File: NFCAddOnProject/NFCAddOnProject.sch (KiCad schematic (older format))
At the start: 30 parts

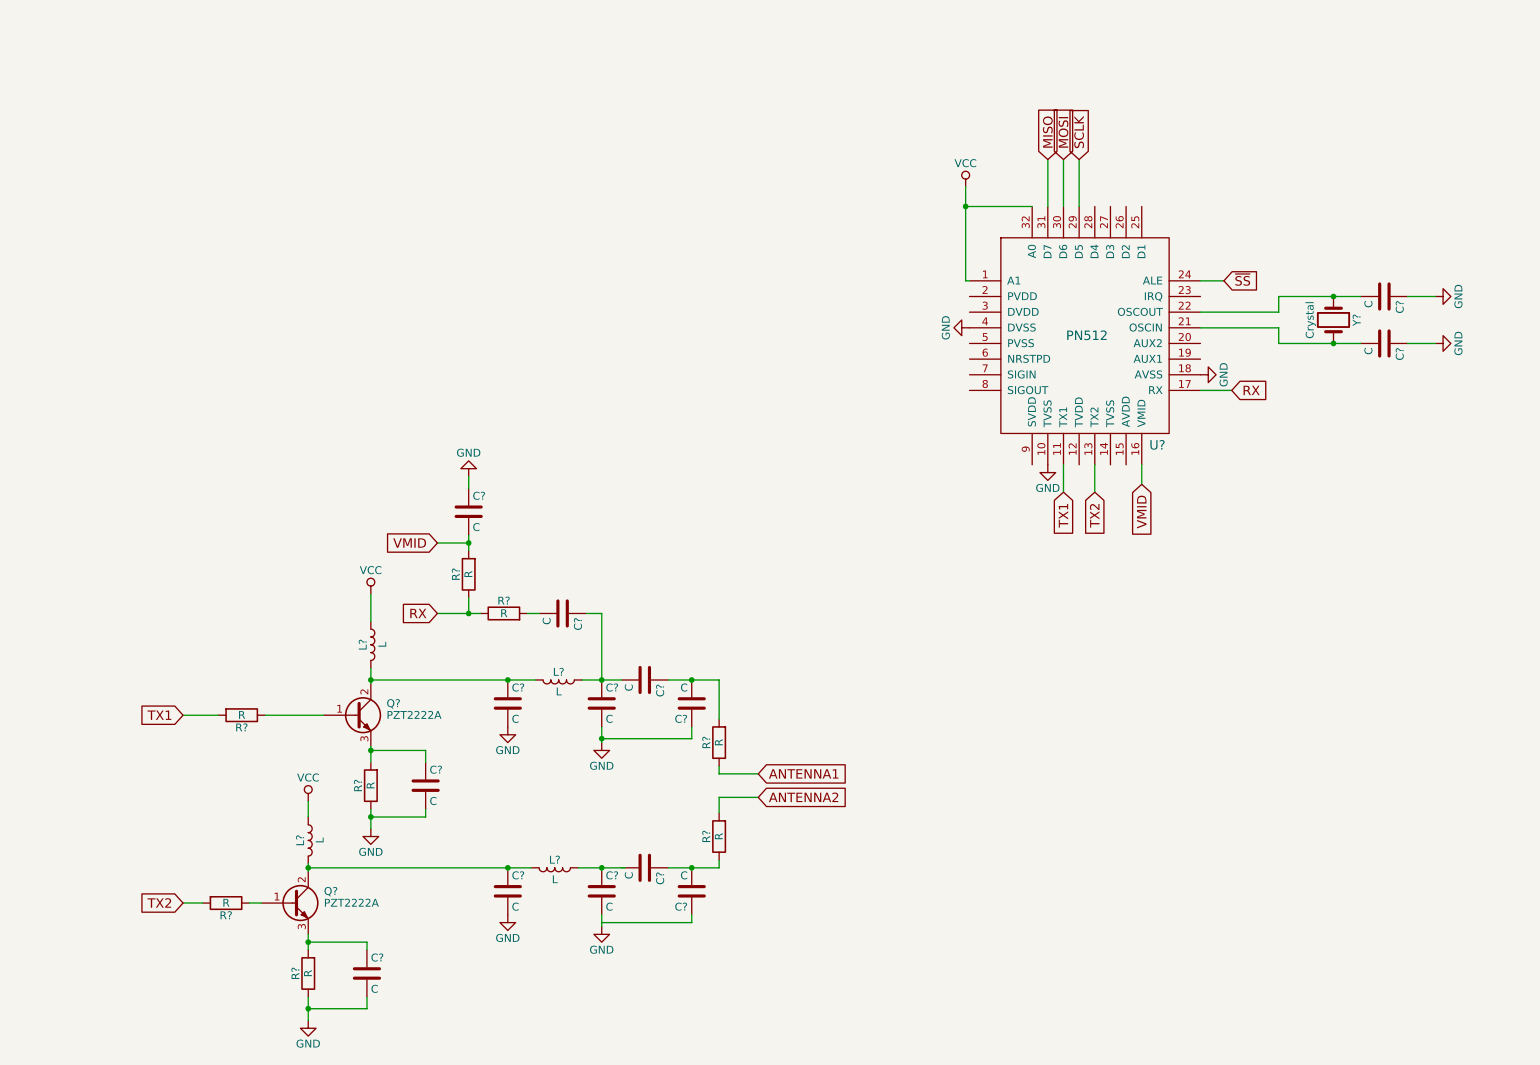
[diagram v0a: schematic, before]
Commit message: Antenna modifications
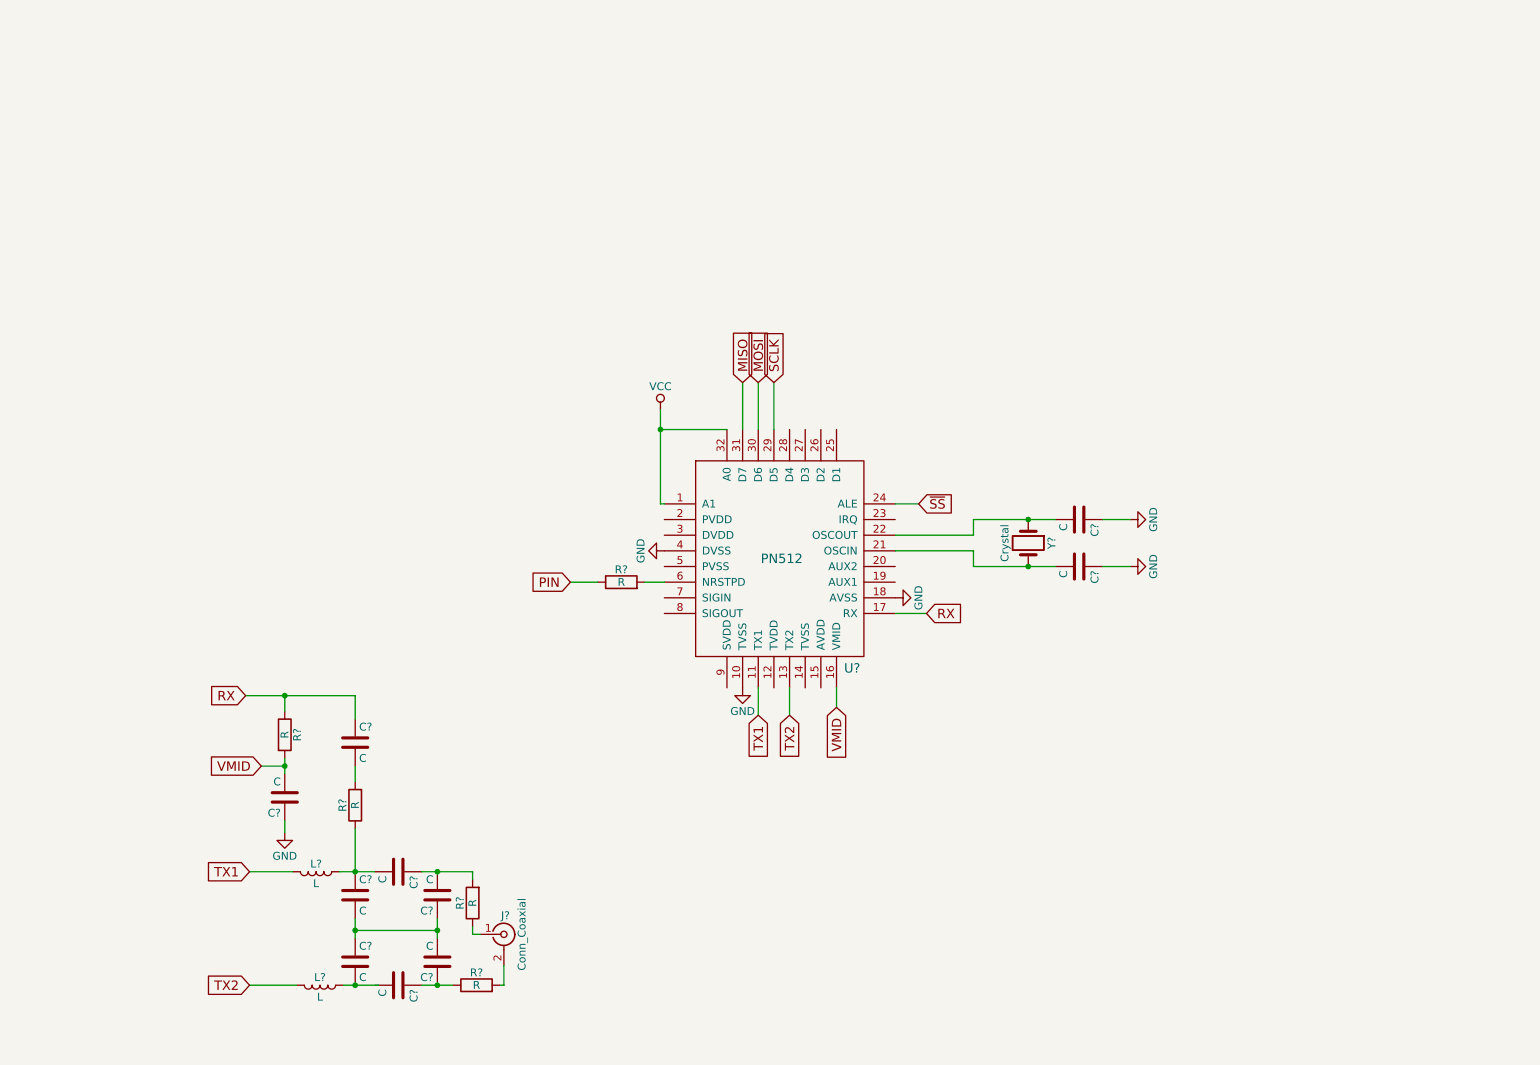
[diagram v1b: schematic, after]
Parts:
- removed C? (x4): C, symbol C
- removed L? (x2): L, symbol L
- removed Q? (x2): PZT2222A, TO_SOT_Packages_SMD:SOT-223, symbol PZT2222A
- removed R? (x4): R, symbol R
- added J?: Conn_Coaxial, symbol Conn_Coaxial
- added R?: R, symbol R
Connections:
- net GND: no longer C?.1, C?.2, C?.2
- net RX: now also C?.1; no longer R?.1
- net TX1: now also L?.2
- net TX2: now also L?.2
- net at U?.6 (NRSTPD): now also R?.2
- net at C?.1, C?.2, L?.1: now also R?.1; no longer C?.1
- net at C?.1, R?.1: now also C?.1; no longer C?.2
- net at L?.1: now also C?.2; no longer C?.1
- net ANTENNA1: no longer names the net of R?.1
- net ANTENNA1: now also J?.1 (In)
- net ANTENNA2: no longer names the net of R?.2
- net ANTENNA2: now also J?.2 (Ext)
- new net: C?.1, C?.1, C?.2, C?.2
- new net PIN: R?.1
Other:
- moved on the sheet: C?, L?, R?, U?, Y?

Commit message: Adding MuxPi-AddOn connector
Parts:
- removed C? (x10): C, symbol C
- removed J?: Conn_Coaxial, symbol Conn_Coaxial
- removed L? (x2): L, symbol L
- removed R? (x4): R, symbol R
- removed Y?: Crystal, symbol Crystal
- added C? (x11): C, symbol C
- added C?: CP1, symbol CP1
- added J?: Conn_Coaxial, symbol Conn_Coaxial
- added J?: CONN_02X08_L, symbol CONN_02X08_L
- added J?: CONN_02X08_R, symbol CONN_02X08_R
- added L? (x2): L, symbol L
- added R? (x6): R, symbol R
- added Y?: Crystal, symbol Crystal
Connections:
- net labels added: IRQ, NRSTPD, TVDD, VDD
- net labels removed: PIN
- wire segments 43 -> 88

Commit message: Finalizing project
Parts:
- removed R? (x3): R, symbol R
- added C12, C9: 12pF, symbol C
- added C15, C16: 39pF, symbol C
- added C17, C21: 100nF, symbol C
- added C18: 1uF, symbol C
- added C22: 100uF/10V, symbol CP1
- added C4, C5: 100pF, symbol C
- added L3: 22nH, symbol L
- added R10, R11: 0, symbol R
- added R3, R6: 4R42, symbol R
- added R7, R8, R9: 10K, symbol R
- C1: renamed from C?; value CP1 -> 10uF/25V
- C10, C11: renamed from C?; value C -> 33pF
- C13, C14: renamed from C?; value C -> 100pF
- C19, C20: renamed from C?; value C -> 15pF
- C2, C3: renamed from C?; value C -> 100nF
- C6: renamed from C?; value C -> 1nF
- C7, C8: renamed from C?; value C -> 56pF
- L1, L2: renamed from L?; value L -> 470nH
- R1: renamed from R?; value R -> 1K
- R2: renamed from R?; value R -> 2.7K
- R4, R5: renamed from R?; value R -> 4R42
- Y1: renamed from Y?; value Crystal -> 27.12MHz
- gave numbers to parts that had none: 4
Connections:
- wire segments 88 -> 126
- no-connect marks 0 -> 20
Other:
- moved on the sheet: C10, C11, C13, C14, C3, C6, J3, L1, L2, R1, R2, R4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

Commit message: Use other library
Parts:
- added U? (x2): PN5120A0HN1/C2.151, SOT:SOT-617-1, symbol PN5120A0HN1/C2.151
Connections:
- wire segments 126 -> 180
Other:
- moved on the sheet: C10, C11, C12, C13, C14, C15, C16, C19, C20, C3, C6, C9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

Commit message: Update schematic
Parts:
- removed U1: PN512, symbol PN512
- added U? (x2): PN5120A0HN1/C2.151, SOT:SOT-617-1, symbol PN5120A0HN1/C2.151
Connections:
- net labels removed: RX, TX1, TX2
- wire segments 180 -> 174
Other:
- moved on the sheet: C19, C20, R10, R11, Y1
